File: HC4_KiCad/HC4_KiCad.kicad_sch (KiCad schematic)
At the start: 0 parts

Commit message: add `jnc` and `jnz` instructions
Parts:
- added C1: C_Polarized, symbol Device:C_Polarized
- added D1: 5.6V, symbol Device:D_Zener
- added D2: POWER_LED, symbol Device:LED
- added J1: Power, symbol Connector:Barrel_Jack
- added R1: 1k, symbol Device:R
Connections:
- new net: D2.1 (K), R1.1
- new net GND: C1.2, D1.2 (A), J1.2, R1.2
- new net VCC: C1.1, D1.1 (K), D2.2 (A), J1.1
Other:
- added sheet ALU (alu.kicad_sch)

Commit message: 進捗コミット
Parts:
- added IC1: RAM, Package_DIP:DIP-28_W15.24mm, symbol Memory_RAM:HM62256BLP
- added IC2: ROM, Package_DIP:DIP-28_W15.24mm, symbol Memory_EPROM:27256
- added RA1: 10k, Resistor_THT:R_Array_SIP5, symbol Device:R_Network04
- C1: value C_Polarized -> 100u
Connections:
- net GND: now also IC1.14 (GND), IC2.14 (GND), IC2.20 (~{CE})
- net VCC: now also IC1.28 (VCC), IC2.1 (VPP), IC2.2 (A12), IC2.26 (A13), IC2.27 (A14), IC2.28 (VCC), RA1.1 (common)
- new net: IC1.16 (Q4), RA1.5 (R4)
- new net: IC1.17 (Q5), RA1.4 (R3)
- new net: IC1.18 (Q6), RA1.3 (R2)
- new net: IC1.19 (Q7), RA1.2 (R1)
- new net Databus0: IC1.11 (Q0)
- new net Databus1: IC1.12 (Q1)
- new net Databus2: IC1.13 (Q2)
- new net Databus3: IC1.15 (Q3)
- new net Instruction_0: IC2.11 (D0)
- new net Instruction_1: IC2.12 (D1)
- new net Instruction_2: IC2.13 (D2)
- new net Instruction_3: IC2.15 (D3)
- new net Instruction_4: IC2.16 (D4)
- new net Instruction_5: IC2.17 (D5)
- new net Instruction_6: IC2.18 (D6)
- new net Instruction_7: IC2.19 (D7)
- new net PC_0: IC2.10 (A0)
- new net PC_1: IC2.9 (A1)
- new net PC_10: IC2.21 (A10)
- new net PC_11: IC2.23 (A11)
- new net PC_2: IC2.8 (A2)
- new net PC_3: IC2.7 (A3)
- new net PC_4: IC2.6 (A4)
- new net PC_5: IC2.5 (A5)
- new net PC_6: IC2.4 (A6)
- new net PC_7: IC2.3 (A7)
- new net PC_8: IC2.25 (A8)
- new net PC_9: IC2.24 (A9)
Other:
- added sheet Address BUS (addressbus.kicad_sch)
- added sheet Data BUS (databus.kicad_sch)
- added sheet Instruction Decoder (instructiondecode.kicad_sch)
- added sheet Program Counter (programcounter.kicad_sch)
- added sheet Stack Unit (stackunit.kicad_sch)
- sheet ALU ports: added ALU_OUT[0..3], ALU_in_A[0..3], ALU_in_B[0..3], ALU_~{Eb}, Carry_IN, Carry_OUT, I1a, I2a, I3a, Sub, ~{Sub}; removed none
- note added: "DATA BUS"

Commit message: 進捗コミット2
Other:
- added sheet Clock and Reset (clockandreset.kicad_sch)
- sheet ALU ports: added I0a; removed Sub, ~{Sub}
- sheet Data BUS ports: added Instruction_[0..7]; removed Immediate[0..3]
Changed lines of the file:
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@@
 	)
 	(junction
+		(at 254 71.12)
+		(diameter 0)
+		(color 0 0 0 0)
+	)
+	(junction
 		(at 36.83 171.45)
 		(diameter 0)
@@
 		)
 	)
+	(bus
+		(pts
+			(xy 254 71.12) (xy 254 93.98)
+		)
+		(stroke
+			(width 0)
+			(type default)
+		)
+	)
 	(wire
 		(pts
@@
 	(bus
 		(pts
-			(xy 254 71.12) (xy 254 93.98)
+			(xy 254 39.37) (xy 254 71.12)
 		)
 		(stroke
@@
 			)
 		)
-		(pin "Immediate[0..3]" input
-			(at 232.41 39.37 270)
-			(effects
-				(font
-					(size 1.27 1.27)
-				)
-				(justify left)
-			)
-		)
 		(pin "Stack[0..3]" output
 			(at 105.41 39.37 270)
@@
 			)
 		)
+		(pin "Instruction_[0..7]" input
+			(at 254 39.37 270)
+			(effects
+				(font
+					(size 1.27 1.27)
+				)
+				(justify left)
+			)
+		)
 		(instances
 			(project "HC4_KiCad"
@@
 	)
 	(sheet
+		(at 248.92 148.59)
+		(size 25.4 11.43)
+		(fields_autoplaced yes)
+		(stroke
+			(width 0.1524)
+			(type solid)
+		)
+		(fill
+			(color 0 0 0 0.0000)
+		)
+		(property "Sheetname" "Clock and Reset"
+			(at 248.92 147.8784 0)
+			(effects
+				(font
+					(size 1.27 1.27)
+				)
+				(justify left bottom)
+			)
+		)
+		(property "Sheetfile" "clockandreset.kicad_sch"
+			(at 248.92 160.6046 0)
+			(effects
+				(font
+					(size 1.27 1.27)
+				)
+				(justify left top)
+			)
+		)
+		(instances
+			(project "HC4_KiCad"
+				(path "/33731ded-38c0-4297-bdd8-92b082f46ff8"
+					(page "8")
+				)
+			)
+		)
+	)
+	(sheet
 		(at 96.52 83.82)
 		(size 46.99 31.75)
@@
 			)
 		)
-		(pin "Sub" input
-			(at 143.51 93.98 0)
-			(effects
-				(font
-					(size 1.27 1.27)
-				)
-				(justify right)
-			)
-		)
 		(pin "I1a" input
 			(at 143.51 100.33 0)
@@
 			)
 		)
-		(pin "~{Sub}" input
-			(at 143.51 96.52 0)
+		(pin "I0a" input
+			(at 143.51 97.79 0)
 			(effects
 				(font

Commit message: I'm tired. あとは任せた　頑張りたまえ
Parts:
- added F1: Polyfuse, Fuse:Fuse_Bourns_MF-RG400, symbol Device:Polyfuse
- added J2: CE, Connector_PinSocket_2.54mm:PinSocket_1x01_P2.54mm_Vertical, symbol Connector:Conn_01x01_Pin
- added JP1: Jumper, Connector_PinHeader_2.54mm:PinHeader_1x03_P2.54mm_Vertical, symbol Jumper:Jumper_3_Bridged12
- added LD26, LD27: LED, LED_THT:LED_Rectangular_W5.0mm_H2.0mm, symbol Device2:LED_
- added R13, R14: 1k, Resistor_THT:R_Axial_DIN0207_L6.3mm_D2.5mm_P7.62mm_Horizontal, symbol Device:R
- added SW1: SW_SPDT, Button_Switch_THT:SW_Slide-03_Wuerth-WS-SLTV_10x2.5x6.4_P2.54mm, symbol Switch:SW_SPDT
- C1: footprint (none) -> Capacitor_THT:CP_Radial_D5.0mm_P2.50mm
- D1: footprint (none) -> Diode_THT:D_DO-34_SOD68_P7.62mm_Horizontal
- J1: footprint (none) -> Connector_BarrelJack:BarrelJack_GCT_DCJ200-10-A_Horizontal
- LD1: renamed from D2; footprint (none) -> LED_THT:LED_D5.0mm; symbol Device:LED -> Device2:LED_
- R1: footprint (none) -> Resistor_THT:R_Axial_DIN0207_L6.3mm_D2.5mm_P7.62mm_Horizontal
- renumbered RA1 to RN1
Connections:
- net ALU/Carry_IN: now also LD27.2
- net GND: now also IC2.22 (~{OE}), R13.2, R14.2, SW1.1 (A)
- net VCC: now also IC1.1 (A14), IC1.2 (A12), IC1.21 (A10), IC1.24 (A9), IC1.25 (A8), IC1.26 (A13), F1.2, JP1.1 (A); no longer J1.1
- net RAM_A0: now reaches IC1.10 (A0)
- net at IC1.20 (~{CS}): now also SW1.2 (B)
- net Address BUS/~{RAM_RD}: now reaches IC1.22 (~{OE})
- net at IC1.23 (A11): now also JP1.2 (C)
- net Address BUS/~{RAM_WR}: now reaches IC1.27 (~{WE})
- net Address BUS/~{RAM_WR}: now also JP1.3 (B)
- net RAM_A7: now reaches IC1.3 (A7)
- net RAM_A6: now reaches IC1.4 (A6)
- net RAM_A5: now reaches IC1.5 (A5)
- net RAM_A4: now reaches IC1.6 (A4)
- net RAM_A3: now reaches IC1.7 (A3)
- net RAM_A2: now reaches IC1.8 (A2)
- net RAM_A1: now reaches IC1.9 (A1)
- new net: J2.1 (Pin_1), SW1.3 (C)
- new net: LD27.1 (K), R14.1
- new net: LD26.1 (K), R13.1
- new net: F1.1, J1.1
- new net Instruction Decoder/Zero_Flg: LD26.2
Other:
- sheet Address BUS ports: added Instruction_[0..7], Level_A[0..3], Level_B[0..3], MEMMode, RAM_A[0..7], READ, ~{RAM_RD}, ~{RAM_WR}; removed none
- sheet Data BUS ports: added BUS_Zero, RAM_A[0..7], ~{RD}, ~{WR}; removed none
- sheet Instruction Decoder ports: added ALU_~{Eb}, BUS_Zero, I0a, I1a, I2a, I3a, MEMMode, READ, Zero_Flg, ~{ALU_OE}, ~{Imm_OE}, ~{LevelC_OE}, ~{STACK_LE}; removed none
- note added: "When using 6116 SRAM, Close 2-3 of JP1"
- moved on the sheet: C1, D1, R1

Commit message: 回路図の修正
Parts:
- added CP23, CP24: 0.1u, Capacitor_THT:C_Disc_D3.0mm_W1.6mm_P2.50mm, symbol Device2:C_Bypass
- renumbered LD26 to LD2, LD27 to LD3, R13 to R2, R14 to R3
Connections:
- net GND: now also CP23.2, CP24.2
- net VCC: now also CP23.1, CP24.1
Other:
- sheet Data BUS ports: added Level_C_OE; removed ~{Level_C_OE}
- sheet Instruction Decoder ports: added LevelC_OE; removed ~{LevelC_OE}
- moved on the sheet: C1, LD1, R1

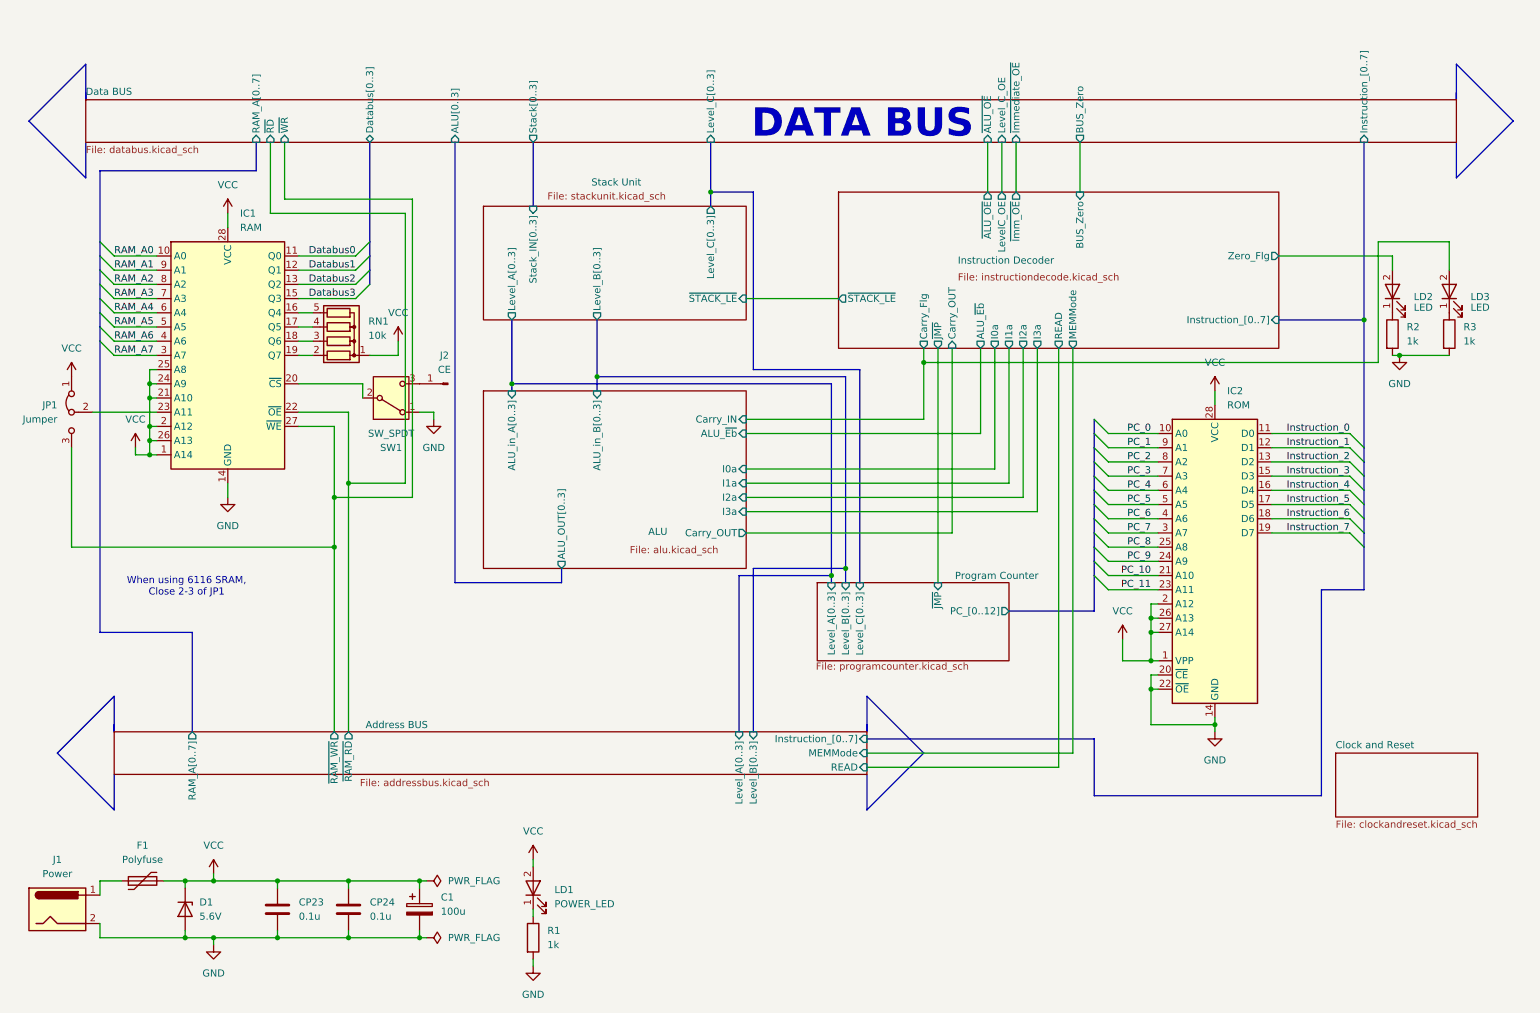
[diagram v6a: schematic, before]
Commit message: ICの配置を再検討
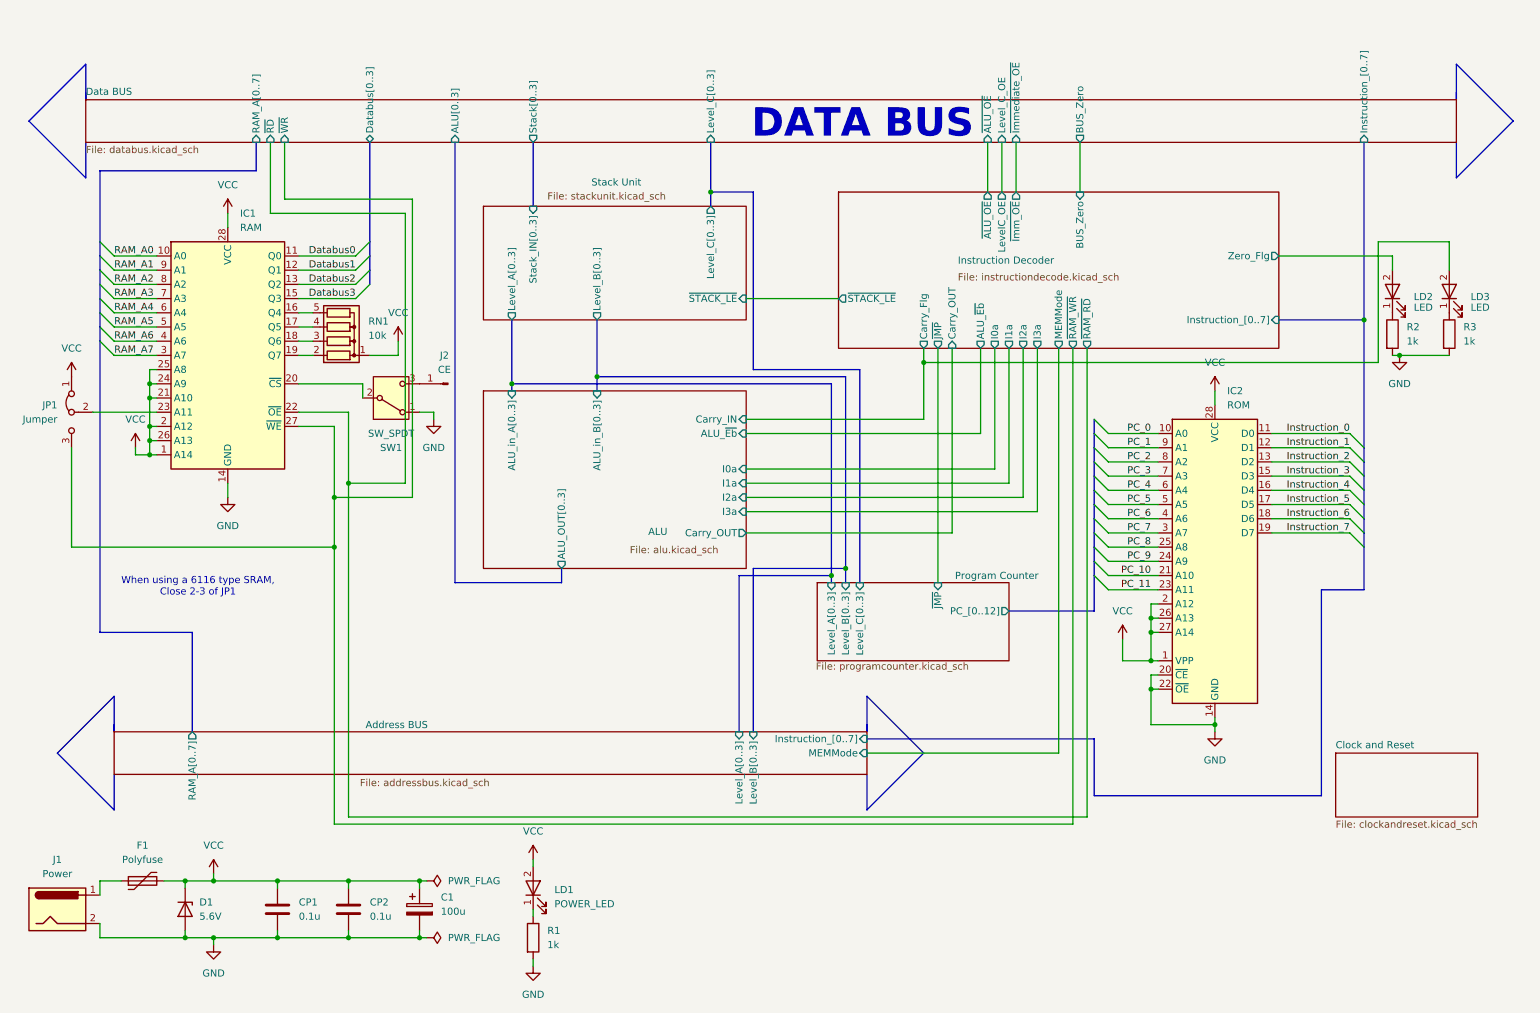
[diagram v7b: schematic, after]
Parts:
- renumbered CP23 to CP1, CP24 to CP2
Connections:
- net Address BUS/~{RAM_RD} renamed Data BUS/~{RD}
- net Address BUS/~{RAM_WR} renamed Data BUS/~{WR}
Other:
- sheet Address BUS ports: added none; removed READ, ~{RAM_RD}, ~{RAM_WR}
- sheet Instruction Decoder ports: added ~{RAM_RD}, ~{RAM_WR}; removed READ
- note added: "When using a 6116 type SRAM, Close 2-3 of JP1"
- note removed: "When using 6116 SRAM, Close 2-3 of JP1"
